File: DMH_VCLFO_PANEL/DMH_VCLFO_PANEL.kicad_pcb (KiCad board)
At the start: 2 copper layers, 100 x 200 mm, 44 parts, among them J0 Panel_GND_Solder_Wire_Pad

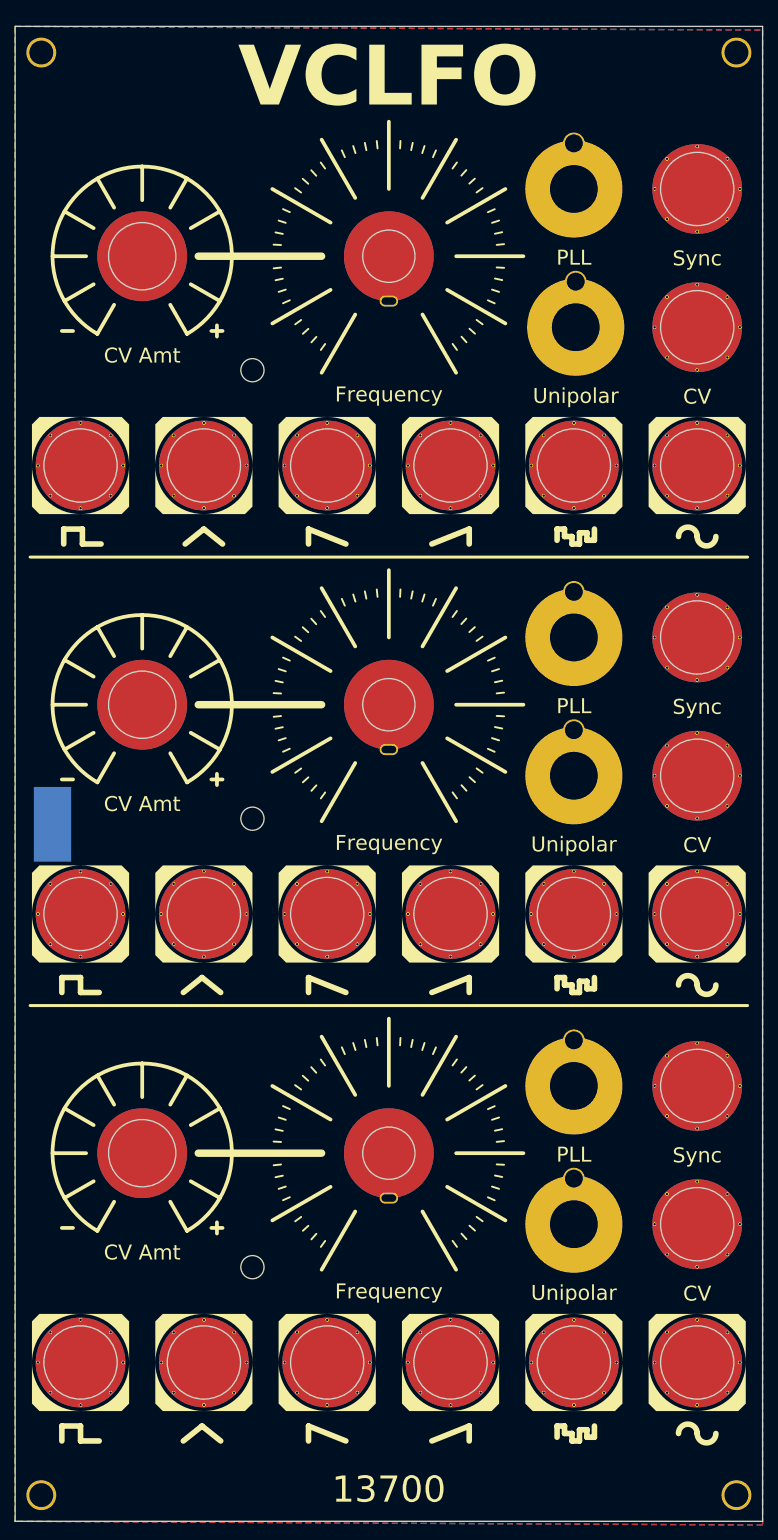
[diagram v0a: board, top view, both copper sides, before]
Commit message: Finished panel v3
Grouped all outputs at the bottom of the module to avoid cables getting in the way of the knobs
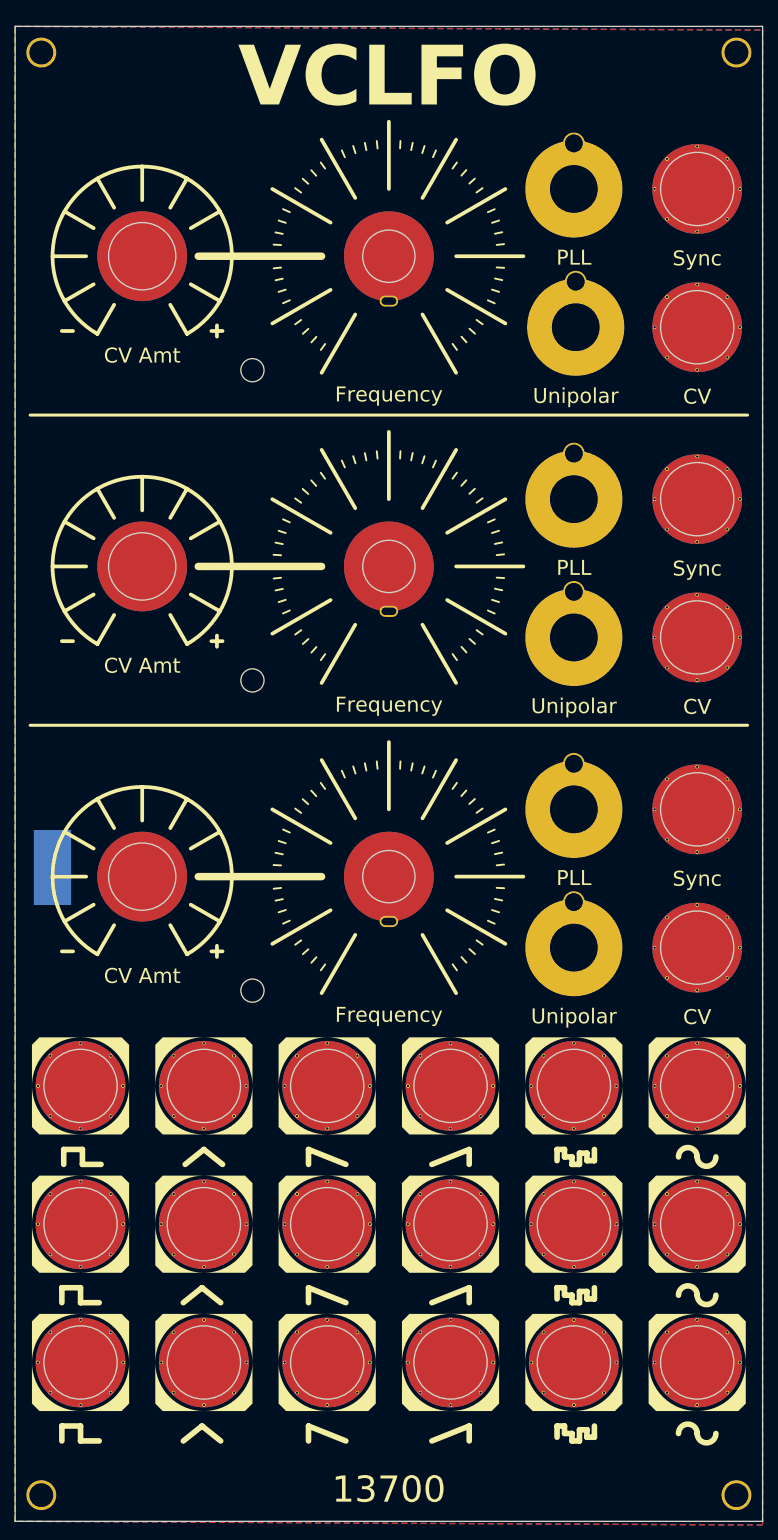
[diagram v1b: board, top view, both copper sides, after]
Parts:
- moved H10 83.0 mm to (124.8, 171.8)
- moved H11 83.0 mm to (141.2, 171.8)
- moved H6 83.0 mm to (58.8, 171.8)
- moved H7 83.0 mm to (75.2, 171.8)
- moved H8 83.0 mm to (91.8, 171.8)
- moved H9 83.0 mm to (108.2, 171.8)
- moved H17 41.5 mm to (58.8, 190.2)
- moved H19 41.5 mm to (75.2, 190.2)
- moved H22 41.5 mm to (108.2, 190.2)
- moved H23 41.5 mm to (124.8, 190.2)
- moved H24 41.5 mm to (141.2, 190.2)
- moved H39 41.5 mm to (91.8, 190.2)
- moved H25 37.0 mm to (81.8, 159.0)
- moved H26 37.0 mm to (100.0, 143.8)
- moved H28 37.0 mm to (67.0, 143.8)
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
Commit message: Improved ergonomics
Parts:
- H10, H23, H33: value Sine -> Ramp / Random
- H11, H24, H34: value Random -> Triangle / Sine
- H17, H27: value Square -> Rmp/Rnd; footprint SynthStuff:Jack_6.35mm_Cutout_Output_v6 -> SynthStuff:Toggle_Switch_TE_Cutout
- H19, H29: value Triangle -> Sin/Tri; footprint SynthStuff:Jack_6.35mm_Cutout_Output_v6 -> SynthStuff:Toggle_Switch_TE_Cutout
- H22, H32, H9: value Ramp -> Saw
- H39, H40, H8: value Saw -> Square
- H44, H45, H46: value Unipolar -> Pol
- H6: value Square -> Sin/Tri; footprint SynthStuff:Jack_6.35mm_Cutout_Output_v6 -> SynthStuff:Toggle_Switch_TE_Cutout
- H7: value Triangle -> Rmp/Rnd; footprint SynthStuff:Jack_6.35mm_Cutout_Output_v6 -> SynthStuff:Toggle_Switch_TE_Cutout
- moved H21 137.0 mm to (75.2, 171.8)
- moved H7 137.0 mm to (141.2, 51.8)
- moved H5 131.0 mm to (58.5, 171.8)
- moved H6 130.8 mm to (141.2, 70.2)
- moved H17 127.3 mm to (141.2, 93.2)
- moved H31 117.3 mm to (75.2, 190.2)
- moved H20 113.9 mm to (58.8, 190.2)
- moved H27 110.8 mm to (141.2, 134.8)
- moved H19 102.6 mm to (141.2, 111.8)
- moved H30 99.4 mm to (58.8, 208.8)
- moved H35 99.2 mm to (75.2, 208.8)
- moved H29 86.2 mm to (141.2, 153.2)
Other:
- board text added: "+"
- board text added: "-"

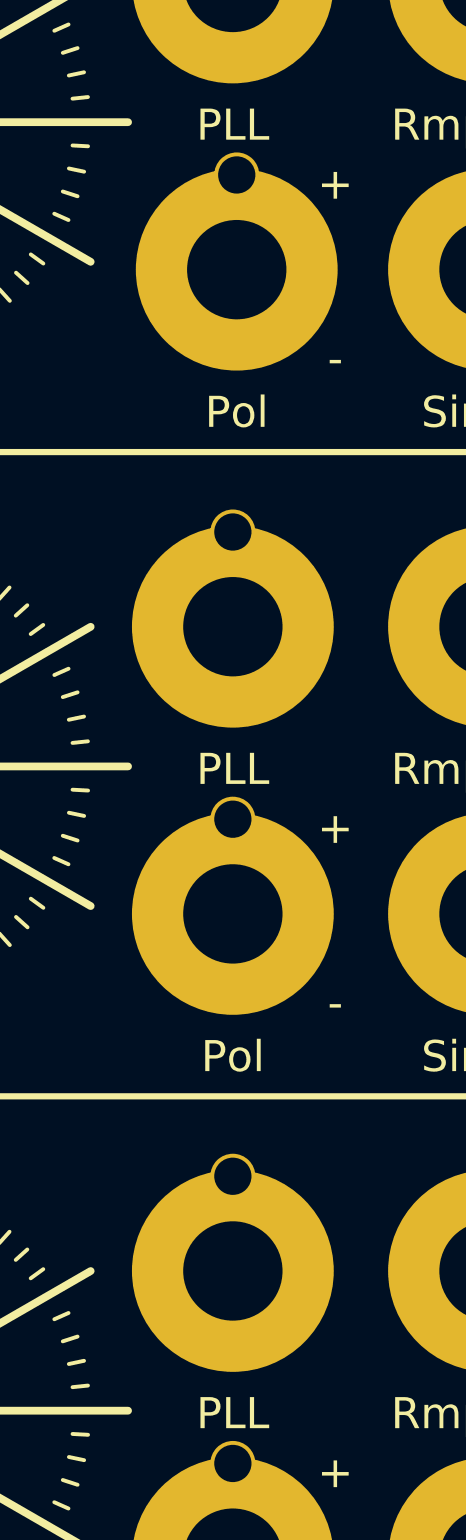
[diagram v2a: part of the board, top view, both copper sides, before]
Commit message: Replaced PLL with Range
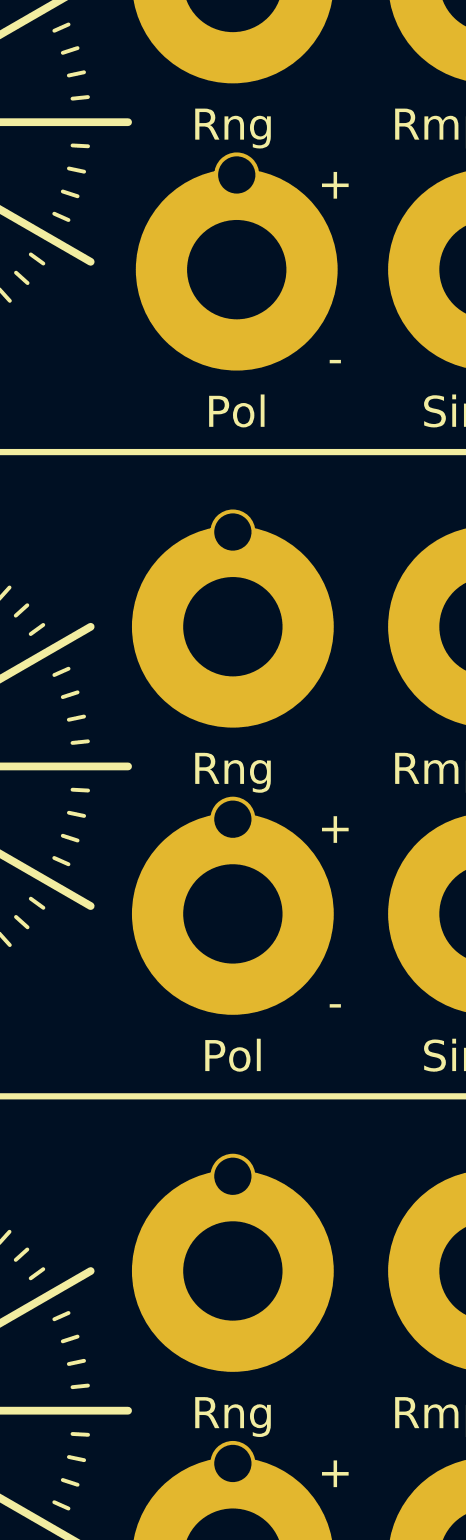
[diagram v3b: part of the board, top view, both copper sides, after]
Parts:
- H41, H42, H43: value PLL -> Rng

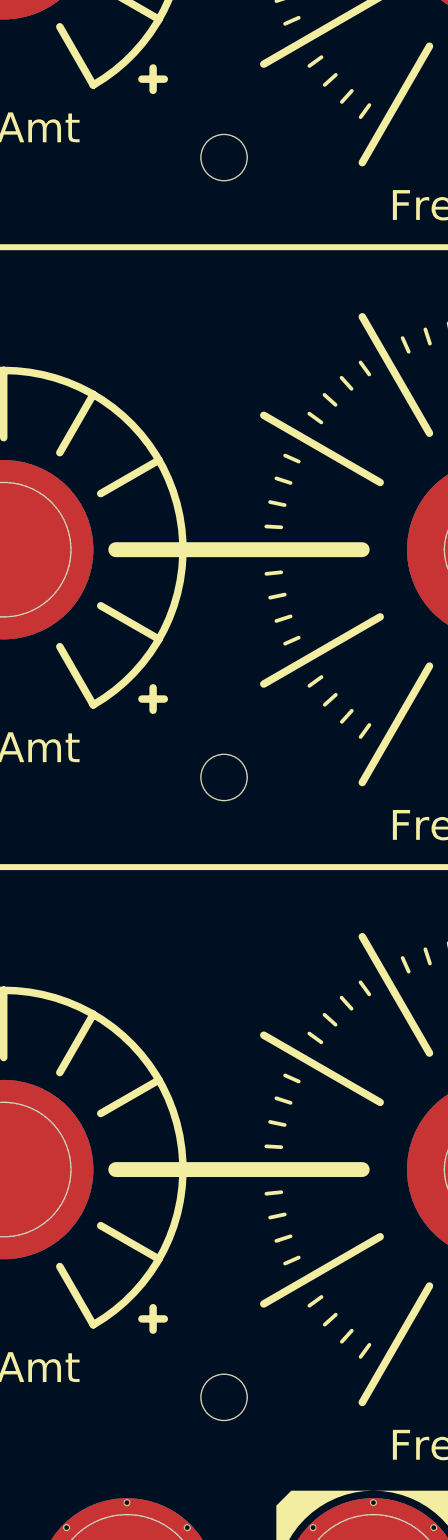
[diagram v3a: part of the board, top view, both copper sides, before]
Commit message: Added yellow LED to Panel
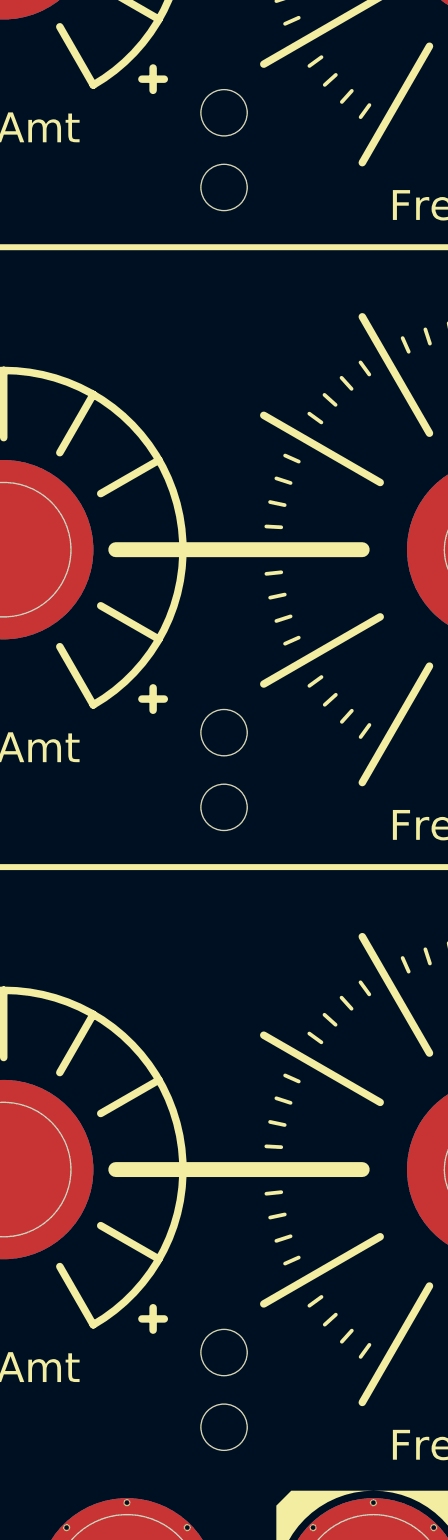
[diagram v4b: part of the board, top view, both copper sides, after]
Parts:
- added H36: LED A Y, SynthStuff:MountingHole_LED_3mm_Y, F.Cu at (81.8, 78.0)
- added H37: LED B Y, SynthStuff:MountingHole_LED_3mm_Y, F.Cu at (81.8, 119.5)
- added H38: LED C Y, SynthStuff:MountingHole_LED_3mm_Y, F.Cu at (81.8, 161.0)
- H14: value LED A -> LED A R; footprint SynthStuff:MountingHole_LED_3mm -> SynthStuff:MountingHole_LED_3mm_R
- H15: value LED A -> LED B R; footprint SynthStuff:MountingHole_LED_3mm -> SynthStuff:MountingHole_LED_3mm_R
- H25: value LED A -> LED C R; footprint SynthStuff:MountingHole_LED_3mm -> SynthStuff:MountingHole_LED_3mm_R
- moved H14 3.00 mm to (81.8, 73.0)
- moved H15 3.00 mm to (81.8, 114.5)
- moved H25 3.00 mm to (81.8, 156.0)

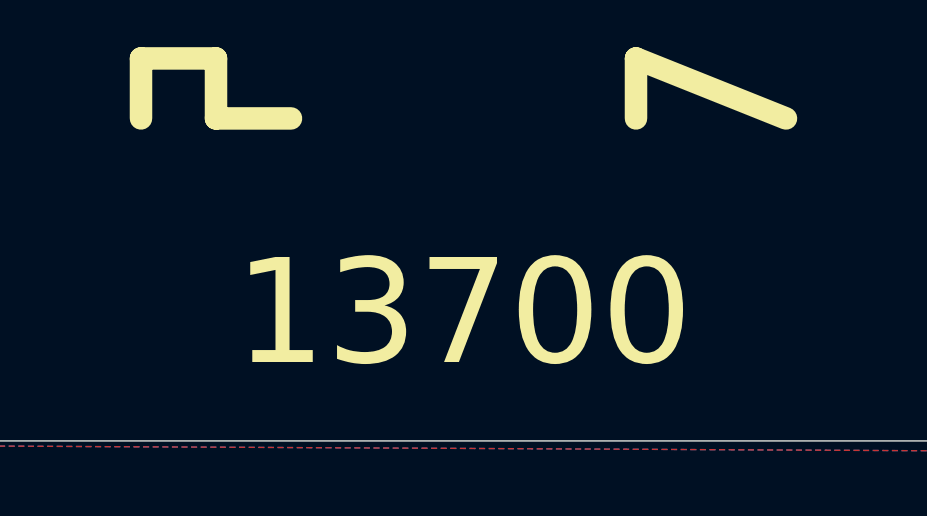
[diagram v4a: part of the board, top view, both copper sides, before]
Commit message: Changed name in panel
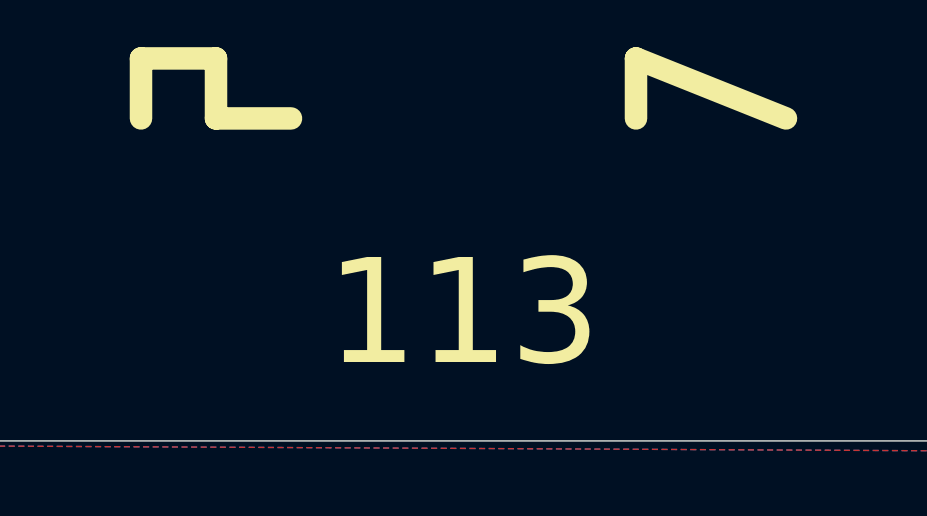
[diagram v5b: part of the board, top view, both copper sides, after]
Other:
- board text added: "113"
- board text removed: "13700"
